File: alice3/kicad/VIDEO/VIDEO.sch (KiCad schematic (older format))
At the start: 17 parts, among them SW1 SW_PUSH, U1 Propeller_P8X32A-D40, U2 VGA_daughter_board, U3 24LC256, U4 Propeller_Plug, U5 LM2937-3.3, U6 74HC4050, U7 74HC4050, U8 Alice_3_bus, Y1 5 MHz

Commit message: Fix video board warnings.
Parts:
- U8: symbol Alice_3_bus-RESCUE-VIDEO -> Alice_3_bus
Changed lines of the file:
@@
 $EndComp
 $Comp
-L Alice_3_bus-RESCUE-VIDEO U8
+L Alice_3_bus U8
 U 1 1 56826E73
 P 1850 5350

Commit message: Start PCB of video board.
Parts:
- C1: footprint (none) -> Discret:CP36V
- D1, D2: footprint (none) -> LEDs:LED-5MM
- R2, R3, R4: footprint (none) -> Resistors_ThroughHole:Resistor_Horizontal_RM10mm
- U2: footprint (none) -> Pin_Headers:Pin_Header_Straight_1x08
- U3: footprint (none) -> Housings_DIP:DIP-8_W7.62mm
- U4: footprint (none) -> Pin_Headers:Pin_Header_Straight_1x04
- U5: footprint (none) -> Power_Integrations:TO-220
- U6, U7: footprint (none) -> Housings_DIP:DIP-16_W7.62mm
- U8: footprint (none) -> Pin_Headers:Pin_Header_Straight_2x10
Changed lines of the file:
@@
 F 0 "U2" H 4950 4350 60  0000 C CNN
 F 1 "VGA_daughter_board" H 5100 3300 60  0000 C CNN
-F 2 "" H 5200 3900 60  0000 C CNN
+F 2 "Pin_Headers:Pin_Header_Straight_1x08" H 5200 3900 60  0001 C CNN
 F 3 "" H 5200 3900 60  0000 C CNN
 	1    5200 3850
@@
 F 0 "U3" H 8650 4450 60  0000 C CNN
 F 1 "24LC256" H 8800 3850 60  0000 C CNN
-F 2 "" H 8900 4050 60  0000 C CNN
+F 2 "Housings_DIP:DIP-8_W7.62mm" H 8900 4050 60  0001 C CNN
 F 3 "" H 8900 4050 60  0000 C CNN
 	1    8900 4150
@@
 F 0 "R2" V 8180 3800 50  0000 C CNN
 F 1 "10k" V 8100 3800 50  0000 C CNN
-F 2 "" V 8030 3800 50  0000 C CNN
+F 2 "Resistors_ThroughHole:Resistor_Horizontal_RM10mm" V 8030 3800 50  0001 C CNN
 F 3 "" H 8100 3800 50  0000 C CNN
 	1    8100 3800
@@
 F 0 "U4" H 9500 3150 60  0000 C CNN
 F 1 "Propeller_Plug" H 9650 2500 60  0000 C CNN
-F 2 "" H 9600 2850 60  0000 C CNN
+F 2 "Pin_Headers:Pin_Header_Straight_1x04" H 9600 2850 60  0001 C CNN
 F 3 "" H 9600 2850 60  0000 C CNN
 	1    9600 2850
@@
 F 0 "U5" H 3650 2650 60  0000 C CNN
 F 1 "LM2937-3.3" H 4100 2650 60  0000 C CNN
-F 2 "" H 3900 2450 60  0000 C CNN
+F 2 "Power_Integrations:TO-220" H 3900 2450 60  0001 C CNN
 F 3 "" H 3900 2450 60  0000 C CNN
 	1    3900 2450
@@
 F 0 "C1" H 4525 2750 50  0000 L CNN
 F 1 "1000 µF" H 4525 2550 50  0000 L CNN
-F 2 "" H 4500 2650 50  0000 C CNN
+F 2 "Discret:CP36V" H 4500 2650 50  0001 C CNN
 F 3 "" H 4500 2650 50  0000 C CNN
 	1    4500 2650
@@
 F 0 "D1" H 5000 2500 50  0000 C CNN
 F 1 "LED" H 5000 2300 50  0000 C CNN
-F 2 "" H 5000 2400 50  0000 C CNN
+F 2 "LEDs:LED-5MM" H 5000 2400 50  0001 C CNN
 F 3 "" H 5000 2400 50  0000 C CNN
 	1    5000 2400
@@
 F 0 "R3" V 5380 2600 50  0000 C CNN
 F 1 "100" V 5300 2600 50  0000 C CNN
-F 2 "" V 5230 2600 50  0000 C CNN
+F 2 "Resistors_ThroughHole:Resistor_Horizontal_RM10mm" V 5230 2600 50  0001 C CNN
 F 3 "" H 5300 2600 50  0000 C CNN
 	1    5300 2600
@@
 F 0 "D2" H 5900 2700 50  0000 C CNN
 F 1 "LED" H 5900 2500 50  0000 C CNN
-F 2 "" H 5900 2600 50  0000 C CNN
+F 2 "LEDs:LED-5MM" H 5900 2600 50  0001 C CNN
 F 3 "" H 5900 2600 50  0000 C CNN
 	1    5900 2600
@@
 F 0 "R4" V 5780 2850 50  0000 C CNN
 F 1 "100" V 5700 2850 50  0000 C CNN
-F 2 "" V 5630 2850 50  0000 C CNN
+F 2 "Resistors_ThroughHole:Resistor_Horizontal_RM10mm" V 5630 2850 50  0001 C CNN
 F 3 "" H 5700 2850 50  0000 C CNN
 	1    5700 2850
@@
 F 0 "U6" H 3350 4850 60  0000 C CNN
 F 1 "74HC4050" H 3900 4850 60  0000 C CNN
-F 2 "" H 3600 4450 60  0000 C CNN
+F 2 "Housings_DIP:DIP-16_W7.62mm" H 3600 4450 60  0001 C CNN
 F 3 "" H 3600 4450 60  0000 C CNN
 	1    3600 4450
@@
 F 0 "U7" H 3350 6650 60  0000 C CNN
 F 1 "74HC4050" H 3900 6650 60  0000 C CNN
-F 2 "" H 3600 6250 60  0000 C CNN
+F 2 "Housings_DIP:DIP-16_W7.62mm" H 3600 6250 60  0001 C CNN
 F 3 "" H 3600 6250 60  0000 C CNN
 	1    3600 6250
@@
 F 0 "U8" H 1650 5900 60  0000 C CNN
 F 1 "Alice_3_bus" H 1850 4800 60  0000 C CNN
-F 2 "" H 1800 5400 60  0000 C CNN
+F 2 "Pin_Headers:Pin_Header_Straight_2x10" H 1800 5400 60  0001 C CNN
 F 3 "" H 1800 5400 60  0000 C CNN
 	1    1850 5350

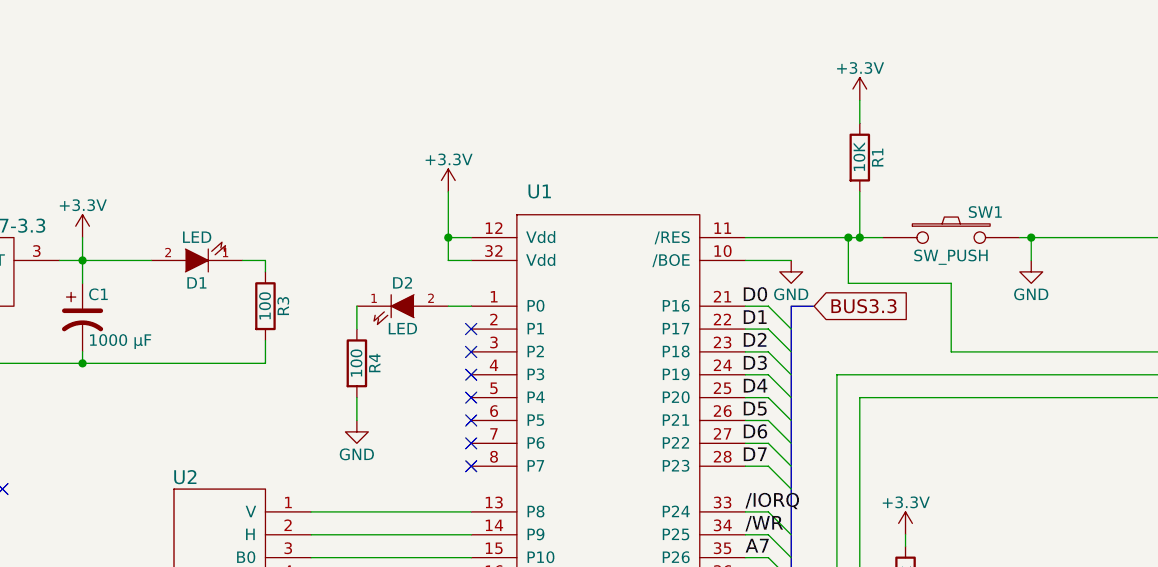
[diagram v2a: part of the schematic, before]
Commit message: Tighten video board PCB.
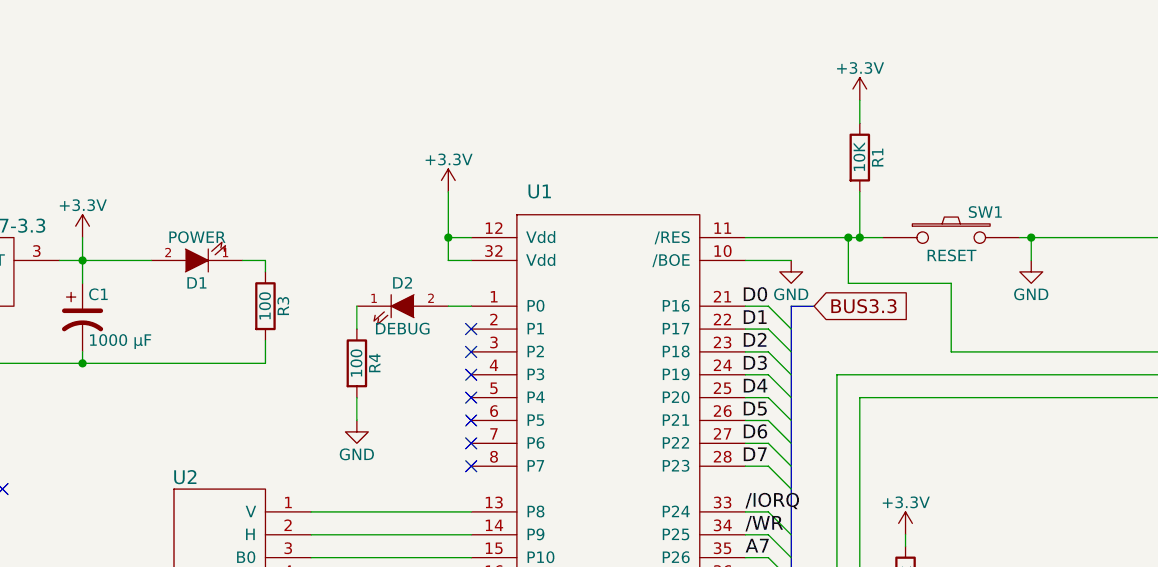
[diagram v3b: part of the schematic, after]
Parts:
- C1: footprint Discret:CP36V -> Capacitors_ThroughHole:C_Radial_D5_L6_P2.5
- D1: value LED -> POWER
- D2: value LED -> DEBUG
- SW1: value SW_PUSH -> RESET
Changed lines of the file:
@@
 P 8300 2300
 F 0 "SW1" H 8450 2410 50  0000 C CNN
-F 1 "SW_PUSH" H 8300 2220 50  0000 C CNN
+F 1 "RESET" H 8300 2220 50  0000 C CNN
 F 2 "Buttons_Switches_ThroughHole:SW_PUSH_SMALL" H 8300 2300 50  0001 C CNN
 F 3 "" H 8300 2300 50  0000 C CNN
@@
 F 0 "C1" H 4525 2750 50  0000 L CNN
 F 1 "1000 µF" H 4525 2550 50  0000 L CNN
-F 2 "Discret:CP36V" H 4500 2650 50  0001 C CNN
+F 2 "Capacitors_ThroughHole:C_Radial_D5_L6_P2.5" H 4500 2650 50  0001 C CNN
 F 3 "" H 4500 2650 50  0000 C CNN
 	1    4500 2650
@@
 P 5000 2400
 F 0 "D1" H 5000 2500 50  0000 C CNN
-F 1 "LED" H 5000 2300 50  0000 C CNN
+F 1 "POWER" H 5000 2300 50  0000 C CNN
 F 2 "LEDs:LED-5MM" H 5000 2400 50  0001 C CNN
 F 3 "" H 5000 2400 50  0000 C CNN
@@
 P 5900 2600
 F 0 "D2" H 5900 2700 50  0000 C CNN
-F 1 "LED" H 5900 2500 50  0000 C CNN
+F 1 "DEBUG" H 5900 2500 50  0000 C CNN
 F 2 "LEDs:LED-5MM" H 5900 2600 50  0001 C CNN
 F 3 "" H 5900 2600 50  0000 C CNN
